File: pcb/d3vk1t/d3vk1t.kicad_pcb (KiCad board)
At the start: 2 copper layers, 100 x 60 mm, 0 parts

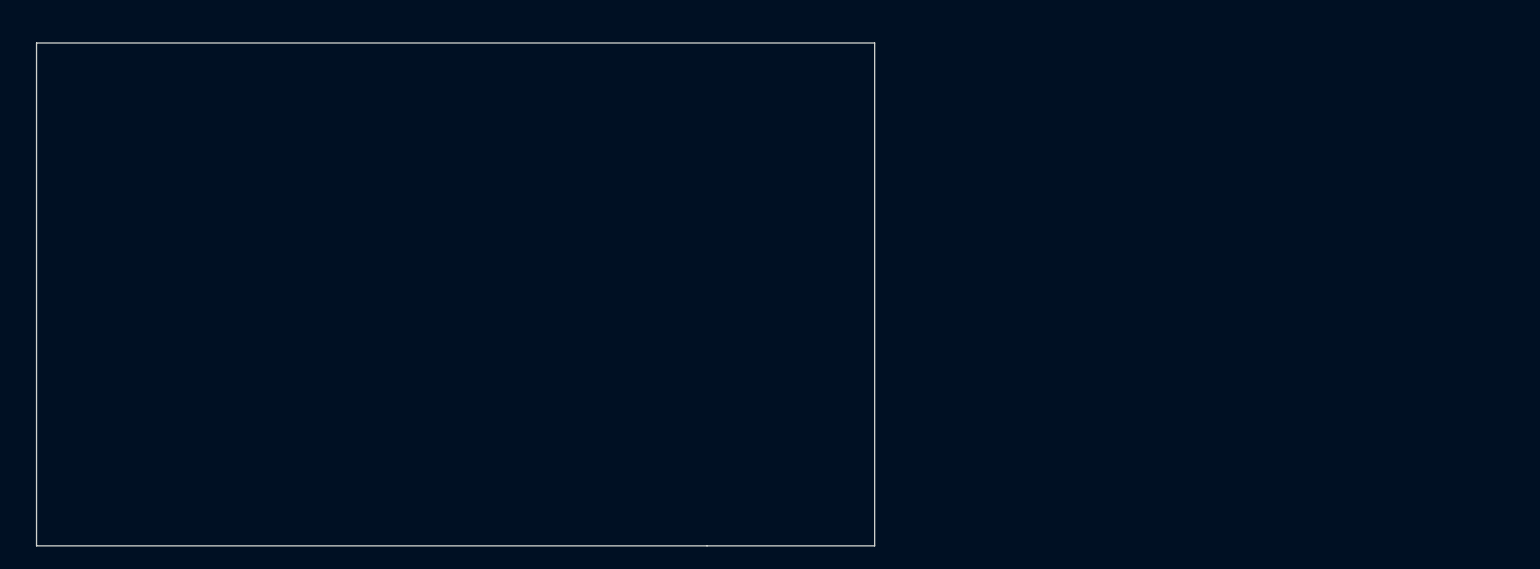
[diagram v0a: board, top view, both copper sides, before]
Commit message: [doc: update mcu pinout, pcb: update board shape]
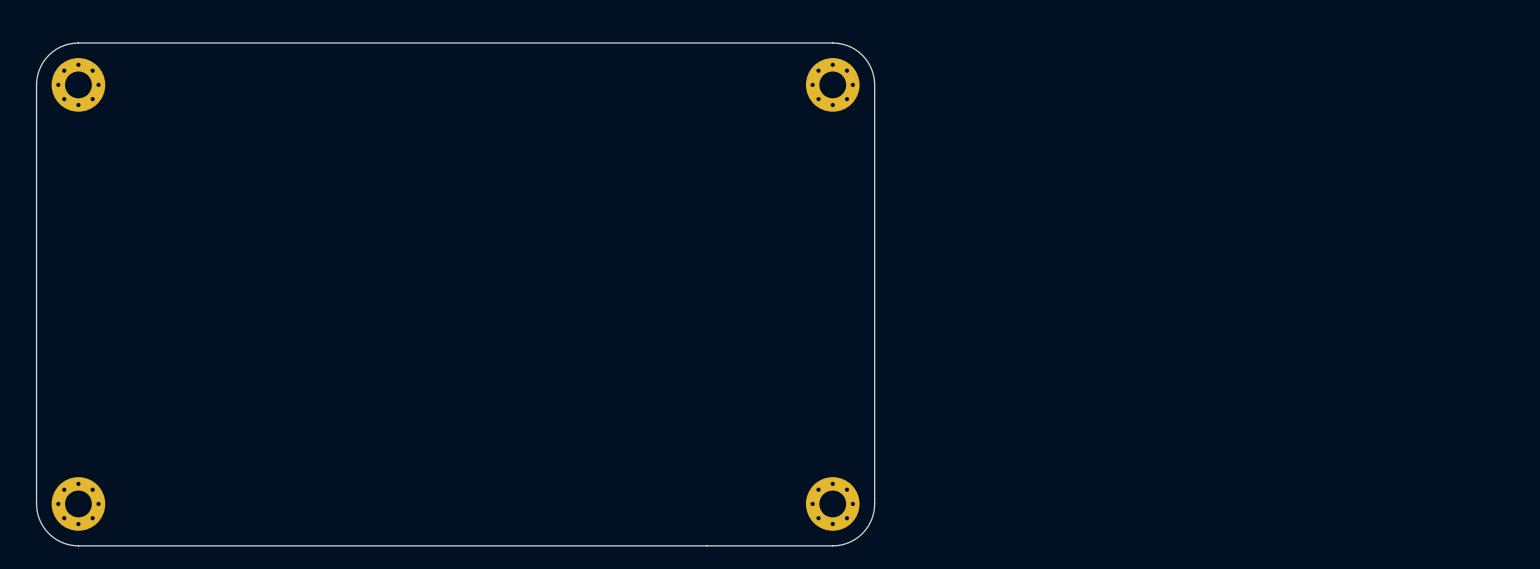
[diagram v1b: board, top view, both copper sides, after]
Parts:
- added H1: MountingHole, MountingHole:MountingHole_3.2mm_M3_Pad_Via, F.Cu at (105.0, 74.0)
- added H2: MountingHole, MountingHole:MountingHole_3.2mm_M3_Pad_Via, F.Cu at (195.0, 74.0)
- added H3: MountingHole, MountingHole:MountingHole_3.2mm_M3_Pad_Via, F.Cu at (195.0, 124.0)
- added H4: MountingHole, MountingHole:MountingHole_3.2mm_M3_Pad_Via, F.Cu at (105.0, 124.0)
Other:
- outline, holes or cut-outs redrawn
- copper layers 2 -> 4

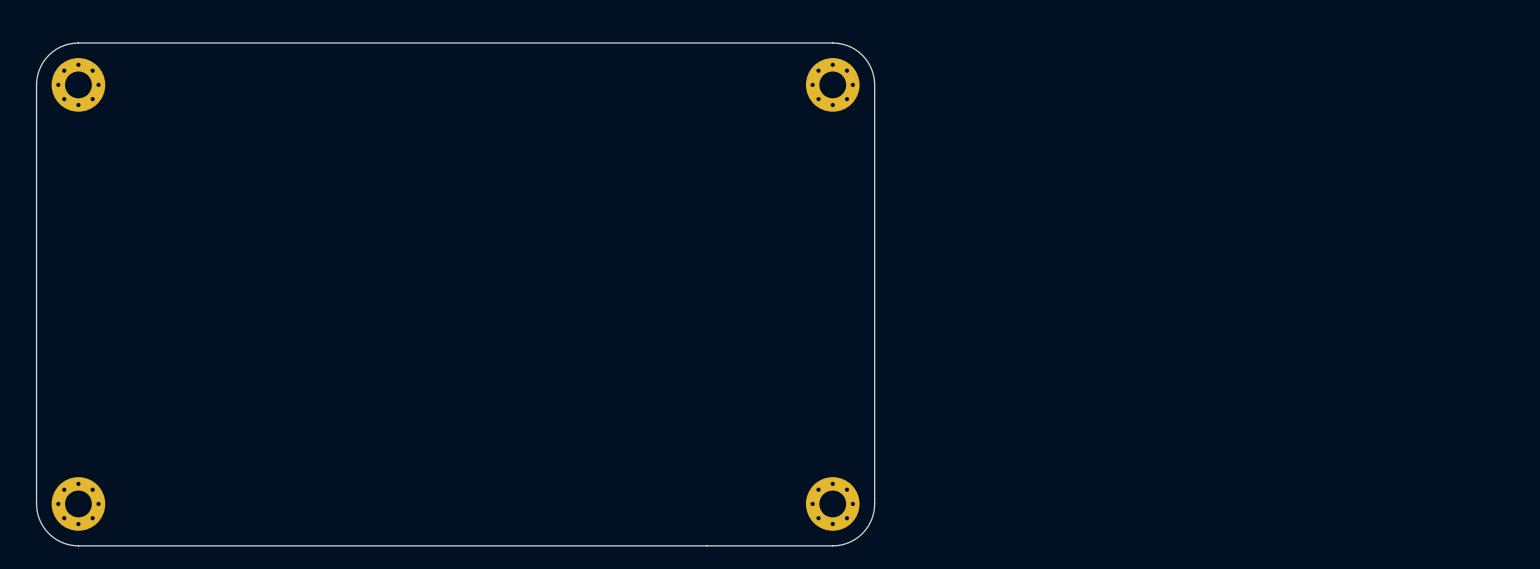
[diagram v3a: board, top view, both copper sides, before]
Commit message: sch: update all sch sheets.
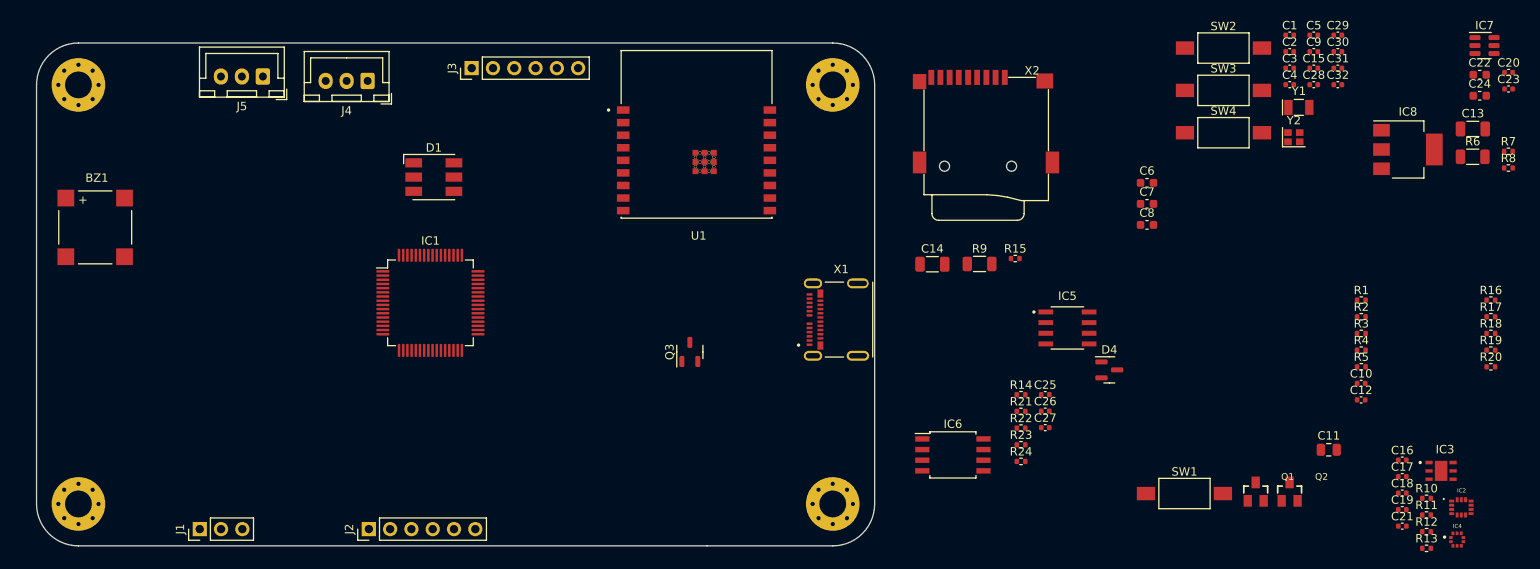
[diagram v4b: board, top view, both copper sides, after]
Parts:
- added BZ1: Buzzer, Buzzer_Beeper:PUIAudio_SMT_0825_S_4_R, F.Cu at (107.0, 91.0)
- added C1: 100nF, Capacitor_SMD:C_0402_1005Metric, F.Cu at (249.5, 68.1)
- added C10: 100nF, Capacitor_SMD:C_0402_1005Metric, F.Cu at (258.0, 109.6)
- added C11: 22uF, Capacitor_SMD:C_0805_2012Metric, F.Cu at (254.2, 117.5)
- added C12: 100nF, Capacitor_SMD:C_0402_1005Metric, F.Cu at (258.0, 111.6)
- added C13: 1nF, Capacitor_SMD:C_1206_3216Metric, F.Cu at (271.4, 79.3)
- added C14: 1nF, Capacitor_SMD:C_1206_3216Metric, F.Cu at (206.9, 95.4)
- added C15: 100nF, Capacitor_SMD:C_0402_1005Metric, F.Cu at (252.4, 72.0)
- added C16: 100nF, Capacitor_SMD:C_0402_1005Metric, F.Cu at (263.0, 118.8)
- added C17: 100nF, Capacitor_SMD:C_0402_1005Metric, F.Cu at (263.0, 120.7)
- added C18: 100nF, Capacitor_SMD:C_0402_1005Metric, F.Cu at (263.0, 122.7)
- added C19: 100nF, Capacitor_SMD:C_0402_1005Metric, F.Cu at (263.0, 124.7)
- added C2: 100nF, Capacitor_SMD:C_0402_1005Metric, F.Cu at (249.5, 70.0)
- added C20: 100nF, Capacitor_SMD:C_0402_1005Metric, F.Cu at (275.6, 72.5)
- added C21: 100nF, Capacitor_SMD:C_0402_1005Metric, F.Cu at (263.0, 126.6)
- added C22: 1uF, Capacitor_SMD:C_0603_1608Metric, F.Cu at (272.2, 72.8)
- added C23: 100nF, Capacitor_SMD:C_0402_1005Metric, F.Cu at (275.6, 74.5)
- added C24: 1uF, Capacitor_SMD:C_0603_1608Metric, F.Cu at (272.2, 75.3)
- added C25: 100nF, Capacitor_SMD:C_0402_1005Metric, F.Cu at (220.4, 111.0)
- added C26: 100nF, Capacitor_SMD:C_0402_1005Metric, F.Cu at (220.4, 112.9)
- added C27: 100nF, Capacitor_SMD:C_0402_1005Metric, F.Cu at (220.4, 114.9)
- added C28: 20pF, Capacitor_SMD:C_0402_1005Metric, F.Cu at (252.4, 74.0)
- added C29: 20pF, Capacitor_SMD:C_0402_1005Metric, F.Cu at (255.3, 68.1)
- added C3: 100nF, Capacitor_SMD:C_0402_1005Metric, F.Cu at (249.5, 72.0)
- added C30: 6.8pF, Capacitor_SMD:C_0402_1005Metric, F.Cu at (255.3, 70.0)
- added C31: 6.8pF, Capacitor_SMD:C_0402_1005Metric, F.Cu at (255.3, 72.0)
- added C32: 100nF, Capacitor_SMD:C_0402_1005Metric, F.Cu at (255.3, 74.0)
- added C4: 100nF, Capacitor_SMD:C_0402_1005Metric, F.Cu at (249.5, 74.0)
- added C5: 100nF, Capacitor_SMD:C_0402_1005Metric, F.Cu at (252.4, 68.1)
- added C6: 1uF, Capacitor_SMD:C_0603_1608Metric, F.Cu at (232.5, 85.7)
- added C7: 4.7uF, Capacitor_SMD:C_0603_1608Metric, F.Cu at (232.5, 88.2)
- added C8: 2.2uF, Capacitor_SMD:C_0603_1608Metric, F.Cu at (232.5, 90.7)
- added C9: 100nF, Capacitor_SMD:C_0402_1005Metric, F.Cu at (252.4, 70.0)
- added D1: LED_RGB, LED_SMD:LED_RGB_5050-6, F.Cu at (147.4, 85.0)
- added D4: SM712-02HTG, Package_TO_SOT_SMD:SOT-23, F.Cu at (228.0, 108.0)
- added IC1: STM32F412RETx, Package_QFP:LQFP-64_10x10mm_P0.5mm, F.Cu at (147.0, 100.0)
- added IC2: LSM6DSMTR, db:PQFN50P300X250X86-14N, F.Cu at (270.0, 124.4)
- added IC3: HDC1080DMBR, db:SON100P300X300X80-7N, F.Cu at (267.6, 120.1)
- added IC4: LPS22HBTR, db:PQFN50P200X200X80-10N, F.Cu at (269.5, 128.3)
- added IC5: TJA1042T/3/1J, db:SOIC127P600X175-8N, F.Cu at (223.0, 103.0)
- added IC6: MAX3485CSA+T, Package_SO:SOIC-8W_5.3x5.3mm_P1.27mm, F.Cu at (209.3, 118.1)
- added IC7: USBLC6-2SC6, Package_TO_SOT_SMD:SOT-23-6, F.Cu at (272.8, 69.3)
- added IC8: LM1117MP-3.3, Package_TO_SOT_SMD:SOT-223-3_TabPin2, F.Cu at (263.6, 81.7)
- added J1: Conn_01x03, Connector_PinHeader_2.54mm:PinHeader_1x03_P2.54mm_Vertical, F.Cu at (119.5, 127.0)
- added J2: Conn_01x06, Connector_PinHeader_2.54mm:PinHeader_1x06_P2.54mm_Vertical, F.Cu at (139.7, 127.0)
- added J3: Conn_01x06, Connector_PinHeader_2.54mm:PinHeader_1x06_P2.54mm_Vertical, F.Cu at (151.9, 72.0)
- added J4: Conn_01x03, Connector_JST:JST_XH_B3B-XH-A_1x03_P2.50mm_Vertical, F.Cu at (139.5, 73.5)
- added J5: Conn_01x03, Connector_JST:JST_XH_B3B-XH-A_1x03_P2.50mm_Vertical, F.Cu at (127.0, 73.0)
- added Q1: MMBT2222, db:SOT23-BEC, F.Cu at (245.5, 122.5)
- added Q2: MMBT2222, db:SOT23-BEC, F.Cu at (249.5, 122.5)
- added Q3: 2N7002, Package_TO_SOT_SMD:SOT-23-3, F.Cu at (177.9, 105.9)
- added R1: 10K, Resistor_SMD:R_0402_1005Metric, F.Cu at (258.1, 99.7)
- added R10: 10K, Resistor_SMD:R_0402_1005Metric, F.Cu at (265.8, 123.3)
- added R11: 10K, Resistor_SMD:R_0402_1005Metric, F.Cu at (265.8, 125.3)
- added R12: 10K, Resistor_SMD:R_0402_1005Metric, F.Cu at (265.8, 127.3)
- added R13: 10K, Resistor_SMD:R_0402_1005Metric, F.Cu at (265.8, 129.3)
- added R14: 10K, Resistor_SMD:R_0402_1005Metric, F.Cu at (217.5, 111.0)
- added R15: 10K, Resistor_SMD:R_0402_1005Metric, F.Cu at (216.8, 94.7)
- added R16: 10K, Resistor_SMD:R_0402_1005Metric, F.Cu at (273.5, 99.7)
- added R17: 1K, Resistor_SMD:R_0402_1005Metric, F.Cu at (273.5, 101.7)
- added R18: 10K, Resistor_SMD:R_0402_1005Metric, F.Cu at (273.5, 103.7)
- added R19: 10K, Resistor_SMD:R_0402_1005Metric, F.Cu at (273.5, 105.6)
- added R2: 10K, Resistor_SMD:R_0402_1005Metric, F.Cu at (258.1, 101.7)
- added R20: 10K, Resistor_SMD:R_0402_1005Metric, F.Cu at (273.5, 107.6)
- added R21: 120R, Resistor_SMD:R_0402_1005Metric, F.Cu at (217.5, 113.0)
- added R22: 0R, Resistor_SMD:R_0402_1005Metric, F.Cu at (217.5, 114.9)
- added R23: 0R, Resistor_SMD:R_0402_1005Metric, F.Cu at (217.5, 116.9)
- added R24: 120R, Resistor_SMD:R_0402_1005Metric, F.Cu at (217.5, 118.9)
- added R3: 10K, Resistor_SMD:R_0402_1005Metric, F.Cu at (258.1, 103.7)
- added R4: 10K, Resistor_SMD:R_0402_1005Metric, F.Cu at (258.1, 105.6)
- added R5: 10K, Resistor_SMD:R_0402_1005Metric, F.Cu at (258.1, 107.6)
- added R6: 1M, Resistor_SMD:R_1206_3216Metric, F.Cu at (271.4, 82.6)
- added R7: 5.1K, Resistor_SMD:R_0402_1005Metric, F.Cu at (275.6, 81.9)
- added R8: 5.1K, Resistor_SMD:R_0402_1005Metric, F.Cu at (275.6, 83.9)
- added R9: 1M, Resistor_SMD:R_1206_3216Metric, F.Cu at (212.5, 95.4)
- added SW1: SW_Push, Button_Switch_SMD:SW_SPST_FSMSM, F.Cu at (237.0, 122.8)
- added SW2: SW_Push, Button_Switch_SMD:SW_SPST_FSMSM, F.Cu at (241.6, 69.6)
- added SW3: SW_Push, Button_Switch_SMD:SW_SPST_FSMSM, F.Cu at (241.6, 74.7)
- added SW4: SW_Push, Button_Switch_SMD:SW_SPST_FSMSM, F.Cu at (241.6, 79.7)
- added U1: ESP32-C3-WROOM-02-H4, db:MODULE_ESP32-C3-WROOM-02-H4, F.Cu at (178.8, 79.9)
- added X1: 105450-0101, db:MOLEX_105450-0101, F.Cu at (196.0, 102.0)
- added X2: Micro_SD_Card_Det, db:microSD_SOFNG_TF-015, F.Cu at (213.3, 74.9)
- added Y1: 32.7680KHZ, Crystal:Crystal_SMD_EuroQuartz_EQ161-2Pin_3.2x1.5mm, F.Cu at (250.6, 76.7)
- added Y2: 24MHz, Crystal:Crystal_SMD_2016-4Pin_2.0x1.6mm, F.Cu at (250.0, 80.2)

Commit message: pcb: update layout
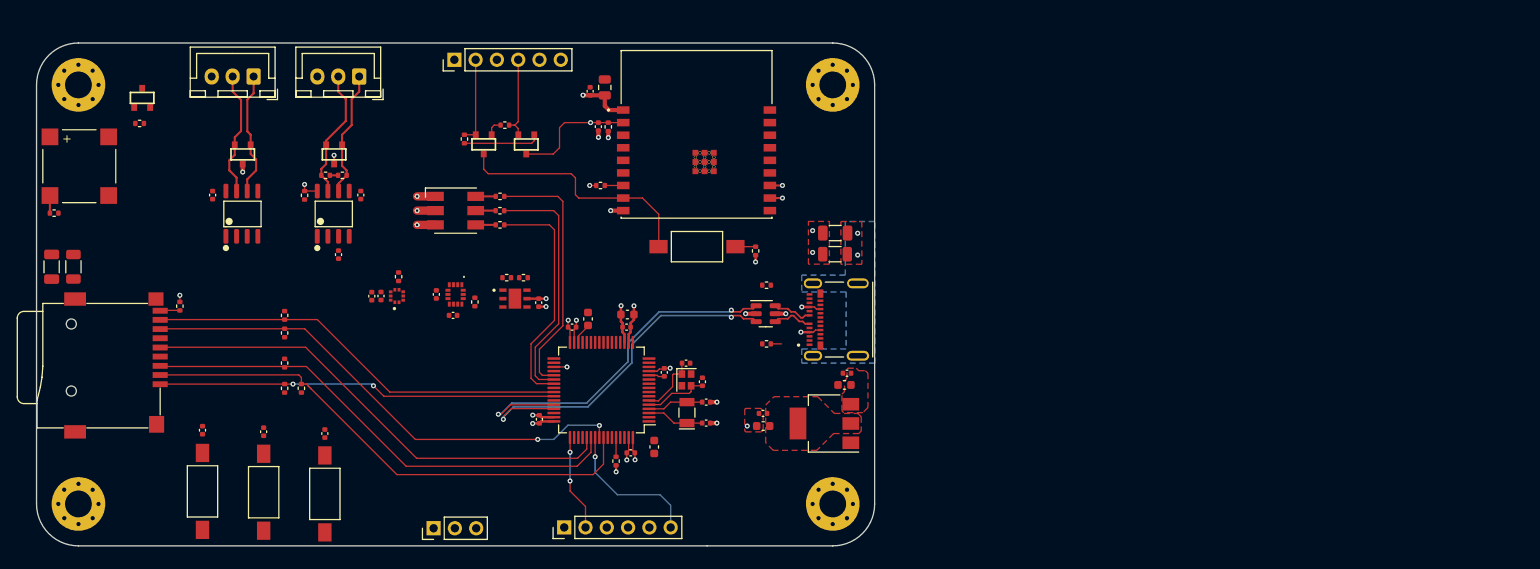
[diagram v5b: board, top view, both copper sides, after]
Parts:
- added D2: PESD2CAN_215, bruno-libs:SOT-23B, F.Cu at (135.5, 82.3)
- added R25: 10K, Resistor_SMD:R_0402_1005Metric, F.Cu at (169.1, 118.9)
- added R26: 47K, Resistor_SMD:R_0402_1005Metric, F.Cu at (129.6, 103.6)
- added R27: 47K, Resistor_SMD:R_0402_1005Metric, F.Cu at (129.6, 101.5)
- added R28: 47K, Resistor_SMD:R_0402_1005Metric, F.Cu at (129.6, 110.2)
- D4: footprint Package_TO_SOT_SMD:SOT-23 -> bruno-libs:SOT-23B
- IC6: footprint Package_SO:SOIC-8W_5.3x5.3mm_P1.27mm -> db:SOIC127P600X175-8N
- Q1, Q2: footprint db:SOT23-BEC -> bruno-libs:SOT-23B
- Q3: footprint Package_TO_SOT_SMD:SOT-23-3 -> bruno-libs:SOT-23B
- R23: value 0R -> 47K
- R24: value 120R -> 47K
- moved R17 171.9 mm to (102.1, 89.3)
- moved R16 162.6 mm to (112.3, 78.6)
- moved C9 140.1 mm to (119.8, 115.2), turned to 90 degrees
- moved SW2 132.8 mm to (119.8, 122.5), turned to 90 degrees
- moved C15 132.6 mm to (127.1, 115.4), turned to 90 degrees
- moved IC4 129.8 mm to (143.0, 99.2), turned to 90 degrees
- moved C32 127.8 mm to (134.4, 115.6), turned to 90 degrees
- moved R11 125.9 mm to (143.2, 96.9), turned to 90 degrees
- moved C19 125.6 mm to (140.0, 99.2), turned to 90 degrees
- moved SW3 124.1 mm to (127.1, 122.6), turned to 90 degrees
- moved C18 124.1 mm to (141.1, 99.2), turned to 90 degrees
- moved IC2 122.7 mm to (150.0, 99.0), turned to -90 degrees
- moved R20 119.4 mm to (155.3, 90.7)
- moved R19 119.4 mm to (155.3, 89.0)
- moved R18 119.4 mm to (155.3, 87.3)
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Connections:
- net Net-(D2-C1) renamed /comm/CAN_H
- net Net-(D2-C2) renamed /comm/CAN_L
- C32 pad 2: GND -> +3.3V
- D4 pad 1: Net-(D4-A1) -> /comm/RS485_B
- D4 pad 2: Net-(D4-A2) -> /comm/RS485_A
- IC6 pad 6: Net-(D4-A1) -> /comm/RS485_B
- IC6 pad 7: Net-(D4-A2) -> /comm/RS485_A
- J5 pad 1: Net-(D4-A2) -> /comm/RS485_B
- J5 pad 2: Net-(D4-A1) -> /comm/RS485_A
- R1 pad 2: Net-(Q1-PadB) -> Net-(Q1-Pad1)
- R2 pad 2: Net-(Q2-PadB) -> Net-(Q2-Pad1)
- R23 pad 1: Net-(R23-Pad1) -> SDIO_D3
- R23 pad 2: Net-(D4-A2) -> +3.3V
- R24 pad 1: Net-(D4-A1) -> SDIO_CMD
- R24 pad 2: Net-(R23-Pad1) -> +3.3V
- SW4 pad 1: GND -> +3.3V
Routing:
- net SDIO_D3: track 0.00 -> 62.6 mm
- net SDIO_D0: track 0.00 -> 60.0 mm, vias 0 -> 2
- net SDIO_CMD: track 0.00 -> 58.7 mm
- net SDIO_CLK: track 0.00 -> 58.2 mm
- net SDIO_D1: track 0.00 -> 50.5 mm
- net SDIO_D2: track 0.00 -> 47.5 mm, vias 0 -> 2
- net USB_N: track 0.00 -> 44.7 mm, vias 0 -> 2
- net USB_P: track 0.00 -> 43.9 mm, vias 0 -> 2
- net GND: track 0.00 -> 30.9 mm, vias 0 -> 20
- net RGB_R: track 0.00 -> 30.7 mm
- net RGB_G: track 0.00 -> 29.4 mm
- net /wifi_ble/GPIO9: track 0.00 -> 29.3 mm
- net RGB_B: track 0.00 -> 28.1 mm
- net +3.3V: track 0.00 -> 26.3 mm, vias 0 -> 10
- net /mcu/SWO: track 0.00 -> 17.4 mm, vias 0 -> 1
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- added copper zone on F.Cu, net +3.3V
- added copper zone on F.Cu, net +5V
- added copper zone on F.Cu, net GND
- added copper zone on In1.Cu, net GND
- added copper zone on In2.Cu, net GND
- added copper zone on B.Cu, net Net-(C13-Pad1)
- added copper zone on F.Cu, net Net-(C13-Pad1)

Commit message: project update  - update pcb layout.  - update schmatics sheets.  - added manufacturing files.  - added documentation files.
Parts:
- added G***: LOGO, LOGO, F.Cu at (182.7, 123.5)
- IC1: value STM32F412RETx -> STM32F412RET6
- R18: value 10K -> 330R
- R19: value 10K -> 470R
- R20: value 10K -> 120R
- moved R17 10.5 mm to (110.6, 83.1), turned to -90 degrees
- moved Q3 8.22 mm to (113.2, 83.7)
- moved R16 7.56 mm to (112.8, 86.2), turned to 180 degrees
- moved J2 4.27 mm to (158.7, 127.1)
- moved C29 2.60 mm to (176.8, 109.7)
- moved C6 1.98 mm to (175.1, 115.8)
- moved Y2 1.50 mm to (178.1, 107.8), turned to 0 degrees
- moved R25 0.48 mm to (169.1, 118.4)
- moved C32 0.40 mm to (134.4, 115.2)
- moved C28 0.32 mm to (179.3, 109.7), turned to 180 degrees
- moved SW2 0.30 mm to (119.8, 122.8)
- moved J1 0.21 mm to (147.3, 127.1)
- moved SW3 0.20 mm to (127.1, 122.8)
- moved C15 0.18 mm to (127.1, 115.2)
- moved BZ1 0.14 mm to (105.2, 83.6), turned to 180 degrees
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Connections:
- net ACC_CS renamed /sensors/ACC_CS
- net ACC_INT renamed /sensors/ACC_INT
- net BARO_CS renamed /sensors/BARO_CS
- net BUZZER renamed /mcu/BUZZER
- net CAN1_RX renamed /comm/CAN1_RX
- net CAN1_TX renamed /comm/CAN1_TX
- net CAN_STB renamed /comm/CAN_STB
- net I2C1_SCL renamed /sensors/I2C1_SCL
- net I2C1_SDA renamed /sensors/I2C1_SDA
- net RGB_B renamed /mcu/RGB_B
- net RGB_G renamed /mcu/RGB_G
- net RGB_R renamed /mcu/RGB_R
- net RS485_DE renamed /comm/RS485_DE
- net SDIO_CLK renamed /mcu/SDIO_CLK
- net SDIO_CMD renamed /mcu/SDIO_CMD
- net SDIO_D0 renamed /mcu/SDIO_D0
- net SDIO_D1 renamed /mcu/SDIO_D1
- net SDIO_D2 renamed /mcu/SDIO_D2
- net SDIO_D3 renamed /mcu/SDIO_D3
- net SDIO_DET renamed /mcu/SDIO_DET
- net SPI1_CLK renamed /sensors/SPI1_CLK
- net SPI1_MISO renamed /sensors/SPI1_MISO
- net SPI1_MOSI renamed /sensors/SPI1_MOSI
- net USART2_RX renamed /mcu/USART2_RX
- net USART2_TX renamed /mcu/USART2_TX
- net USART3_RX renamed /mcu/USART3_RX
- net USART3_TX renamed /mcu/USART3_TX
- net USB_N renamed /mcu/USB_N
- net USB_P renamed /mcu/USB_P
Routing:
- net +5V: track 6.03 -> 163.0 mm, vias 3 -> 7
- net /mcu/SDIO_DET: track 2.35 -> 93.8 mm, vias 0 -> 2
- net /mcu/BUZZER: track 1.57 -> 90.4 mm, vias 1 -> 2
- net /mcu/NRST: track 0.00 -> 81.5 mm
- net /mcu/USER: track 0.00 -> 77.2 mm, vias 0 -> 3
- net /comm/RS485_DE: track 0.00 -> 64.6 mm, vias 0 -> 2
- net /mcu/USART3_RX: track 0.00 -> 64.1 mm, vias 0 -> 2
- net /mcu/SDIO_D3: track 62.6 -> 126.4 mm
- net /sensors/I2C1_SDA: track 0.00 -> 56.4 mm, vias 0 -> 4
- net /comm/CAN_STB: track 2.30 -> 58.4 mm, vias 1 -> 2
- net /comm/CAN1_TX: track 0.00 -> 55.4 mm, vias 0 -> 2
- net /sensors/I2C1_SCL: track 0.00 -> 54.3 mm, vias 0 -> 4
- net /mcu/USART3_TX: track 0.00 -> 53.9 mm, vias 0 -> 2
- net GND: track 30.9 -> 82.0 mm, vias 20 -> 56
- net /sensors/SPI1_CLK: track 0.00 -> 50.4 mm, vias 0 -> 2
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- added copper zone on In2.Cu, net +3.3V
- added copper zone on B.Cu, net +5V
- added copper zone on F.Cu, net Net-(X2-SHIELD)
- removed copper zone on In2.Cu, net GND
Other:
- board text added: "BOOT"
- board text added: "CAN"
- board text added: "Designed By: Gustavo Adono"
- board text added: "ESP FLASH"
- board text added: "GND"
- board text added: "IN"
- board text added: "OUT"
- board text added: "RGB"
- board text added: "RS485"
- board text added: "RST"
- board text added: "SWD"
- board text added: "USER"
